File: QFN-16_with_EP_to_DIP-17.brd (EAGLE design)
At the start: 22.9 x 10.2 mm, 3 parts, among them J1 CONNECTOR_8, J2 CONNECTOR_9, U1 QFN-16_WITH_EP-QFN-16_EP

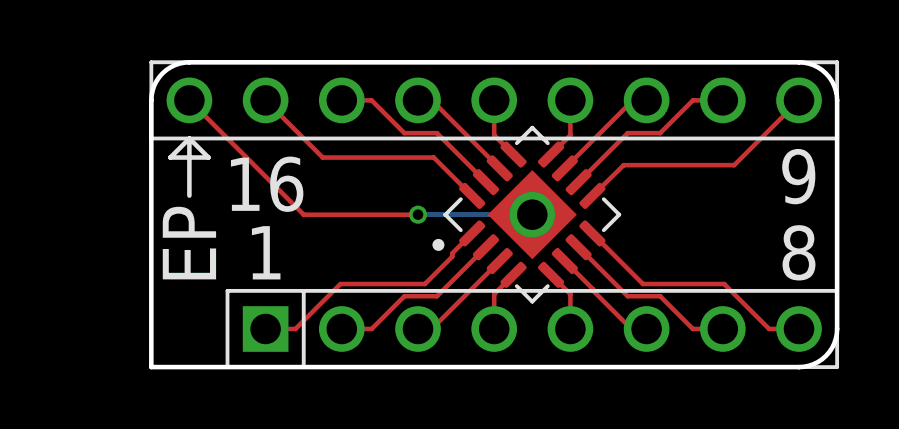
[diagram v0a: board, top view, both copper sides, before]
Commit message: Rerouted QFN-16 PCB.  Thicker traces, board outline changed to 0 width.
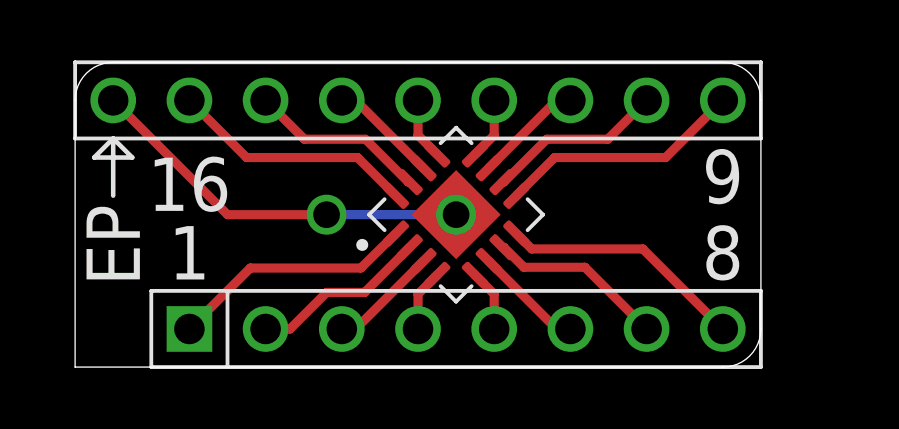
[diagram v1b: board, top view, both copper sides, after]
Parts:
- moved U1 2.54 mm to (12.7, 5.08)
- moved J1 2.54 mm to (3.81, 1.27)
- moved J2 2.54 mm to (21.6, 8.89)
